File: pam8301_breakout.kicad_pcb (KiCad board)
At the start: 2 copper layers, 20 x 11 mm, 10 parts, among them J1 Conn_01x04, J2 Conn_01x02, U1 PAM8301

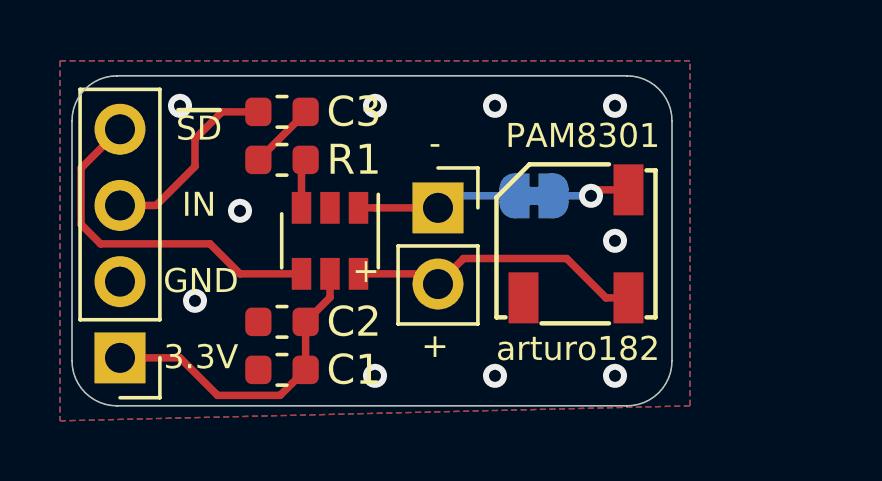
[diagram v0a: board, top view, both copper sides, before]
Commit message: Change to 7.5mm speaker
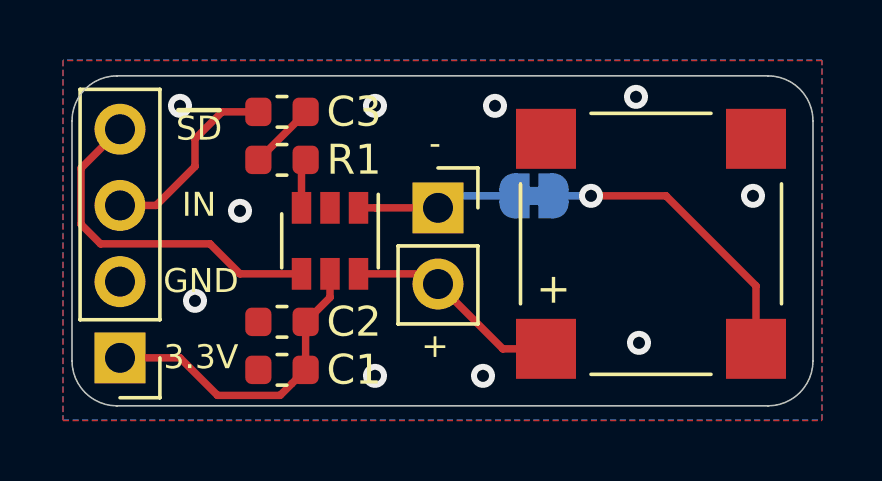
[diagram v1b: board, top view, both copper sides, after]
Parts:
- LS1: footprint Buzzer_Beeper_Extra:CMT-5023S -> Buzzer_Beeper:PUIAudio_SMT_0825_S_4_R
- moved LS1 2.50 mm to (142.7, 79.6)
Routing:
- net Net-(JP1-Pad2): track 2.58 -> 10.1 mm
- net Net-(J2-Pad2): track 10.0 -> 7.29 mm
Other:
- board size 20 x 11 mm -> 24.7 x 11 mm
